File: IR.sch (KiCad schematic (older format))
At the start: 15 parts

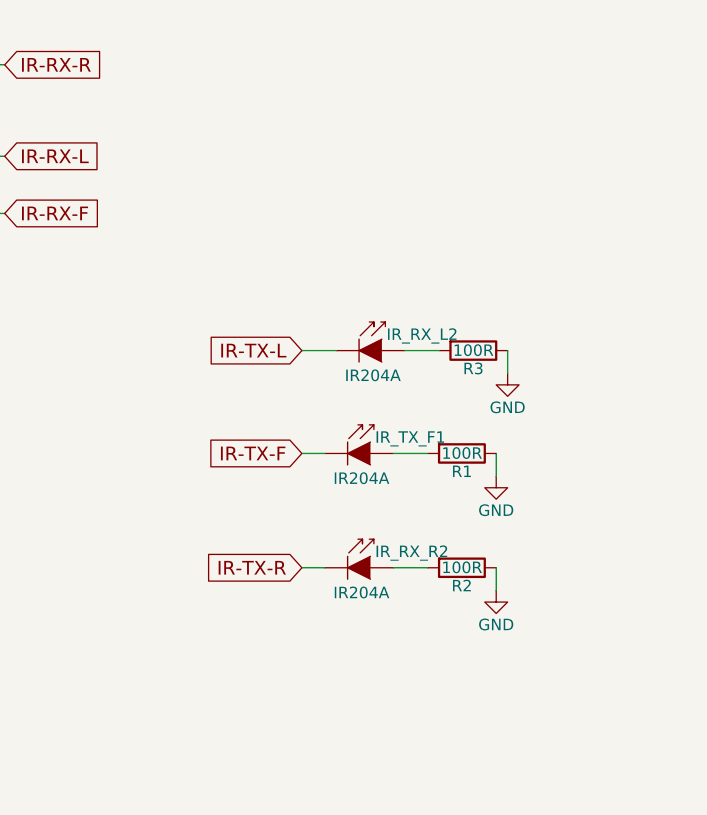
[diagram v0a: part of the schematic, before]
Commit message: IR fixes + routing fixes
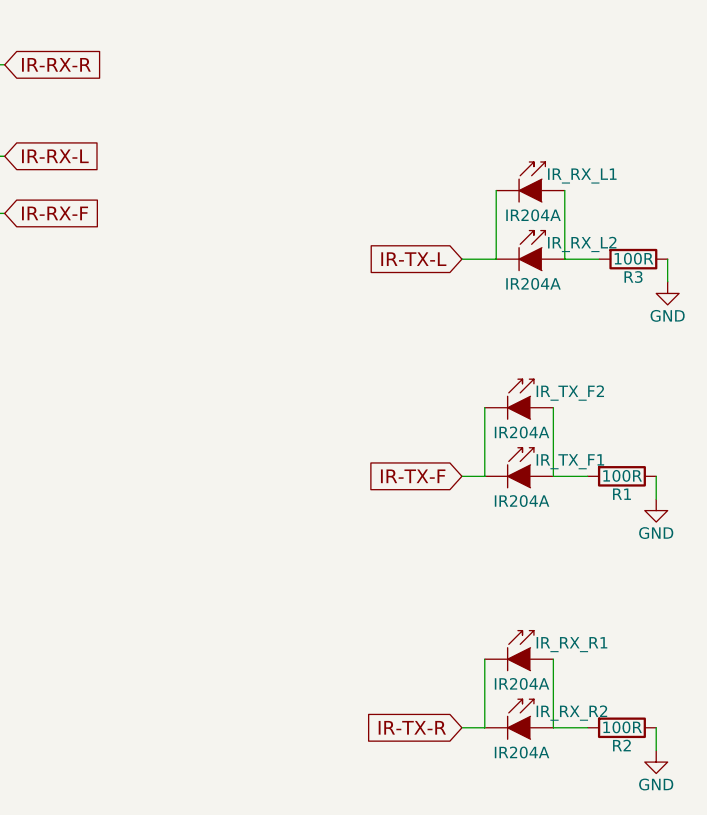
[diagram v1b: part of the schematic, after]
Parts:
- added IR_RX_L1, IR_RX_R1, IR_TX_F2: IR204A, custom-footprints:OSRAM-Midled, symbol IR204A
- IR_RX_L2, IR_RX_R2, IR_TX_F1: footprint LEDs:LED_0603 -> custom-footprints:OSRAM-Midled
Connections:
- wire segments 40 -> 46
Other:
- moved on the sheet: IR_RX_L2, IR_RX_R2, IR_TX_F1, R1, R2, R3
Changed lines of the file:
@@
 $EndDescr
 $Comp
-L GND #PWR1229
+L GND #PWR01229
 U 1 1 5B14512F
 P 4900 4750
-F 0 "#PWR1229" H 4900 4500 50  0001 C CNN
+F 0 "#PWR01229" H 4900 4500 50  0001 C CNN
 F 1 "GND" H 4900 4600 50  0000 C CNN
 F 2 "" H 4900 4750 50  0001 C CNN
@@
 L IR204A IR_TX_F1
 U 1 1 5B145135
-P 7450 4350
-F 0 "IR_TX_F1" H 7470 4420 50  0000 L CNN
-F 1 "IR204A" H 7410 4240 50  0000 C CNN
-F 2 "LEDs:LED_0603" H 7450 4525 50  0001 C CNN
-F 3 "" H 7400 4350 50  0000 C CNN
-	1    7450 4350
+P 8150 4450
+F 0 "IR_TX_F1" H 8170 4520 50  0000 L CNN
+F 1 "IR204A" H 8110 4340 50  0000 C CNN
+F 2 "custom-footprints:OSRAM-Midled" H 8150 4625 50  0001 C CNN
+F 3 "" H 8100 4450 50  0000 C CNN
+	1    8150 4450
 	1    0    0    -1
 $EndComp
@@
 L IR204A IR_RX_L2
 U 1 1 5B14513C
-P 7500 3900
-F 0 "IR_RX_L2" H 7520 3970 50  0000 L CNN
-F 1 "IR204A" H 7460 3790 50  0000 C CNN
-F 2 "LEDs:LED_0603" H 7500 4075 50  0001 C CNN
-F 3 "" H 7450 3900 50  0000 C CNN
-	1    7500 3900
+P 8200 3500
+F 0 "IR_RX_L2" H 8220 3570 50  0000 L CNN
+F 1 "IR204A" H 8160 3390 50  0000 C CNN
+F 2 "custom-footprints:OSRAM-Midled" H 8200 3675 50  0001 C CNN
+F 3 "" H 8150 3500 50  0000 C CNN
+	1    8200 3500
 	1    0    0    -1
 $EndComp
@@
 L IR204A IR_RX_R2
 U 1 1 5B145143
-P 7450 4850
-F 0 "IR_RX_R2" H 7470 4920 50  0000 L CNN
-F 1 "IR204A" H 7410 4740 50  0000 C CNN
-F 2 "LEDs:LED_0603" H 7450 5025 50  0001 C CNN
-F 3 "" H 7400 4850 50  0000 C CNN
-	1    7450 4850
+P 8150 5550
+F 0 "IR_RX_R2" H 8170 5620 50  0000 L CNN
+F 1 "IR204A" H 8110 5440 50  0000 C CNN
+F 2 "custom-footprints:OSRAM-Midled" H 8150 5725 50  0001 C CNN
+F 3 "" H 8100 5550 50  0000 C CNN
+	1    8150 5550
 	1    0    0    -1
 $EndComp
@@
 L R R1
 U 1 1 5B14514A
-P 7850 4350
-F 0 "R1" V 7930 4350 50  0000 C CNN
-F 1 "100R" V 7850 4350 50  0000 C CNN
-F 2 "Resistors_SMD:R_0603" V 7780 4350 50  0001 C CNN
-F 3 "" H 7850 4350 50  0001 C CNN
-	1    7850 4350
+P 8550 4450
+F 0 "R1" V 8630 4450 50  0000 C CNN
+F 1 "100R" V 8550 4450 50  0000 C CNN
+F 2 "Resistors_SMD:R_0603" V 8480 4450 50  0001 C CNN
+F 3 "" H 8550 4450 50  0001 C CNN
+	1    8550 4450
 	0    1    1    0
 $EndComp
@@
 L R R3
 U 1 1 5B145151
-P 7900 3900
-F 0 "R3" V 7980 3900 50  0000 C CNN
-F 1 "100R" V 7900 3900 50  0000 C CNN
-F 2 "Resistors_SMD:R_0603" V 7830 3900 50  0001 C CNN
-F 3 "" H 7900 3900 50  0001 C CNN
-	1    7900 3900
+P 8600 3500
+F 0 "R3" V 8680 3500 50  0000 C CNN
+F 1 "100R" V 8600 3500 50  0000 C CNN
+F 2 "Resistors_SMD:R_0603" V 8530 3500 50  0001 C CNN
+F 3 "" H 8600 3500 50  0001 C CNN
+	1    8600 3500
 	0    1    1    0
 $EndComp
@@
 L R R2
 U 1 1 5B145158
-P 7850 4850
-F 0 "R2" V 7930 4850 50  0000 C CNN
-F 1 "100R" V 7850 4850 50  0000 C CNN
-F 2 "Resistors_SMD:R_0603" V 7780 4850 50  0001 C CNN
-F 3 "" H 7850 4850 50  0001 C CNN
-	1    7850 4850
-	0    1    1    0
-$EndComp
-$Comp
-L GND #PWR1231
-U 1 1 5B14515F
-P 8000 4450
-F 0 "#PWR1231" H 8000 4200 50  0001 C CNN
-F 1 "GND" H 8000 4300 50  0000 C CNN
-F 2 "" H 8000 4450 50  0001 C CNN
-F 3 "" H 8000 4450 50  0001 C CNN
-	1    8000 4450
-	1    0    0    -1
-$EndComp
-$Comp
-L GND #PWR1233
+P 8550 5550
+F 0 "R2" V 8630 5550 50  0000 C CNN
+F 1 "100R" V 8550 5550 50  0000 C CNN
+F 2 "Resistors_SMD:R_0603" V 8480 5550 50  0001 C CNN
+F 3 "" H 8550 5550 50  0001 C CNN
+	1    8550 5550
+	0    1    1    0
+$EndComp
+$Comp
+L GND #PWR01231
 U 1 1 5B145165
-P 8050 4000
-F 0 "#PWR1233" H 8050 3750 50  0001 C CNN
-F 1 "GND" H 8050 3850 50  0000 C CNN
-F 2 "" H 8050 4000 50  0001 C CNN
-F 3 "" H 8050 4000 50  0001 C CNN
-	1    8050 4000
-	1    0    0    -1
-$EndComp
-$Comp
-L GND #PWR1232
+P 8750 3600
+F 0 "#PWR01231" H 8750 3350 50  0001 C CNN
+F 1 "GND" H 8750 3450 50  0000 C CNN
+F 2 "" H 8750 3600 50  0001 C CNN
+F 3 "" H 8750 3600 50  0001 C CNN
+	1    8750 3600
+	1    0    0    -1
+$EndComp
+$Comp
+L GND #PWR01232
 U 1 1 5B14516B
-P 8000 4950
-F 0 "#PWR1232" H 8000 4700 50  0001 C CNN
-F 1 "GND" H 8000 4800 50  0000 C CNN
-F 2 "" H 8000 4950 50  0001 C CNN
-F 3 "" H 8000 4950 50  0001 C CNN
-	1    8000 4950
+P 8700 5650
+F 0 "#PWR01232" H 8700 5400 50  0001 C CNN
+F 1 "GND" H 8700 5500 50  0000 C CNN
+F 2 "" H 8700 5650 50  0001 C CNN
+F 3 "" H 8700 5650 50  0001 C CNN
+	1    8700 5650
 	1    0    0    -1
 $EndComp
@@
 	2150 4750 4900 4750
 Wire Wire Line
-	8000 4350 8000 4450
-Wire Wire Line
-	8050 3900 8050 4000
-Wire Wire Line
-	8000 4850 8000 4950
-Wire Wire Line
-	7550 4350 7700 4350
-Wire Wire Line
-	7600 3900 7750 3900
-Wire Wire Line
-	7550 4850 7700 4850
-$Comp
-L +3.3V #PWR1230
+	8700 4450 8700 4550
+Wire Wire Line
+	8750 3500 8750 3600
+Wire Wire Line
+	8700 5550 8700 5650
+Wire Wire Line
+	8250 4450 8400 4450
+Wire Wire Line
+	8300 3500 8450 3500
+Wire Wire Line
+	8250 5550 8400 5550
+$Comp
+L +3.3V #PWR01233
 U 1 1 5B14519E
 P 4900 5100
-F 0 "#PWR1230" H 4900 4950 50  0001 C CNN
+F 0 "#PWR01233" H 4900 4950 50  0001 C CNN
 F 1 "+3.3V" H 4900 5240 50  0000 C CNN
 F 2 "" H 4900 5100 50  0001 C CNN
@@
 Text GLabel 5850 3300 2    60   Input ~ 0
 IR-RX-F
-Text GLabel 7150 3900 0    60   Input ~ 0
+Text GLabel 7850 3500 0    60   Input ~ 0
 IR-TX-L
-Text GLabel 7150 4350 0    60   Input ~ 0
+Text GLabel 7850 4450 0    60   Input ~ 0
 IR-TX-F
-Text GLabel 7150 4850 0    60   Input ~ 0
+Text GLabel 7850 5550 0    60   Input ~ 0
 IR-TX-R
 Wire Wire Line
-	7150 3900 7300 3900
-Wire Wire Line
-	7150 4350 7250 4350
-Wire Wire Line
-	7150 4850 7250 4850
+	7850 3500 8000 3500
+Wire Wire Line
+	7850 4450 7950 4450
+Wire Wire Line
+	7850 5550 7950 5550
 $Comp
 L R_Small R23
@@
 	1600 2750 1350 2750
 Connection ~ 1350 2750
+$Comp
+L IR204A IR_RX_L1
+U 1 1 5B183598
+P 8200 3200
+F 0 "IR_RX_L1" H 8220 3270 50  0000 L CNN
+F 1 "IR204A" H 8160 3090 50  0000 C CNN
+F 2 "custom-footprints:OSRAM-Midled" H 8200 3375 50  0001 C CNN
+F 3 "" H 8150 3200 50  0000 C CNN
+	1    8200 3200
+	1    0    0    -1
+$EndComp
+Wire Wire Line
+	8000 3500 8000 3200
+Wire Wire Line
+	8300 3200 8300 3500
+$Comp
+L IR204A IR_TX_F2
+U 1 1 5B18399B
+P 8150 4150
+F 0 "IR_TX_F2" H 8170 4220 50  0000 L CNN
+F 1 "IR204A" H 8110 4040 50  0000 C CNN
+F 2 "custom-footprints:OSRAM-Midled" H 8150 4325 50  0001 C CNN
+F 3 "" H 8100 4150 50  0000 C CNN
+	1    8150 4150
+	1    0    0    -1
+$EndComp
+$Comp
+L IR204A IR_RX_R1
+U 1 1 5B1839EA
+P 8150 5250
+F 0 "IR_RX_R1" H 8170 5320 50  0000 L CNN
+F 1 "IR204A" H 8110 5140 50  0000 C CNN
+F 2 "custom-footprints:OSRAM-Midled" H 8150 5425 50  0001 C CNN
+F 3 "" H 8100 5250 50  0000 C CNN
+	1    8150 5250
+	1    0    0    -1
+$EndComp
+Wire Wire Line
+	7950 4450 7950 4150
+Wire Wire Line
+	8250 4150 8250 4450
+Wire Wire Line
+	7950 5550 7950 5250
+Wire Wire Line
+	8250 5250 8250 5550
+$Comp
+L GND #PWR?
+U 1 1 5B1854F9
+P 8700 4550
+F 0 "#PWR?" H 8700 4300 50  0001 C CNN
+F 1 "GND" H 8700 4400 50  0000 C CNN
+F 2 "" H 8700 4550 50  0001 C CNN
+F 3 "" H 8700 4550 50  0001 C CNN
+	1    8700 4550
+	1    0    0    -1
+$EndComp
 $EndSCHEMATC
